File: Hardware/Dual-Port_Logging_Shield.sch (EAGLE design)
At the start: 87 parts, among them IC1 USB224X_2241, J2 MICRO-SD-PUSH-PUSH-EXT-PIN, J3 AVR_SPI_PROG_3X2TESTPOINTS, J4 THING_PLUS, Q1 20V/4.2A/52mΩ/1.4W, Q2 20V/0.2A/8MHz/1.2Ω/1Vth, Q3 20V/4.2A/52mΩ/1.4W, Q4 20V/4.2A/52mΩ/1.4W, Q6 20V/4.2A/52mΩ/1.4W, U1 3.3V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

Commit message: Final Eagle files for Proto
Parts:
- added D+, D-, MICROSD_VCC, V_USB: TEST-POINT3, SparkFun-Connectors:TEST-POINT3
- added D3: PRTR5V0U2F, SparkFun-IC-Power:PRTR5V0U2F
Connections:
- new net D+_IN: D+.1, D3.6, J1.D+
- new net D-_IN: D-.1, D3.4, J1.D-
- net D+: now also D3.1; no longer J1.D+
- net D-: now also D3.3; no longer J1.D-
- net GND: now also D3.2
- net MICROSD_VCC: now also MICROSD_VCC.1
- net V_USB: now also D3.5, V_USB.1
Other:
- note added: "Default I2C Address (Unshifted): 0x51 Address is programmable"
- note added: "USB Differential Pair: Conductor Width: 8.8 mils Conductor Spacing (center to center): 15 mils Conductor Spacing (gap): 6.2 mils Prepreg Thickness: 0.2 mm (7.87 mils) Zdifferential: 90.1 Ohms https://saturnpcb.com/saturn-pcb-toolkit/"
- moved on the sheet: C13, C6, C7, D1, D2, GND, I2C, J1, J3, LED1, LED2, R10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

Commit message: Updates post proto review
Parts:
- added R26, R27, R28: 100, SparkFun-Resistors:100OHM-0402-TIGHT-1/16W-1%
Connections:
- removed net AT_CIPO: J3.1, U3.(CIPO/A5)5
- new net AT_POCI: J3.1, U3.(POCI/A5)5
- new net N$6: Q3.G, R26.2, R9.1
- new net N$7: Q2.G, R20.2, R27.1
- new net N$8: Q2.D, R28.1
- net MICROSD_PWR_EN: now also R26.1; no longer Q3.G, R9.1
- net N$17: now also R28.2; no longer Q2.D
- net SDA: now also U3.(SDA/PICO/A6)6; no longer U3.(SDA/COPI/A6)6
- net SDIO_EN: now also R27.2; no longer Q2.G, R20.2
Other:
- note added: "v01"
- note removed: "v10"
- moved on the sheet: C5, C9, J2, Q2, Q3, R15, R20, R9, U4

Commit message: Add v10 hardware files
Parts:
- removed SD_WP: TEST-POINT3, SparkFun-Connectors:TEST-POINT3
- added R29, R30: 10k, SparkFun-Resistors:10KOHM-0402T-1/16W-1%
- added SH: JUMPER-SMT_2_NC_TRACE_SILK, SparkFun-Jumpers:JUMPER-SMT_2_NC_TRACE_SILK
- D+, D-, GND, V_USB: value TEST-POINT3 -> TEST-POINT3X5; device SparkFun-Connectors:TEST-POINT3 -> SparkFun-Connectors:TEST-POINT3X5
- IC1: value USB224X_2241 -> USB224X_2241_V04; device USB224x:USB224X_2241 -> SparkFun-IC-Special-Function:USB224X_2241_V04
- R21, R23: value 10k -> 100k; device SparkFun-Resistors:10KOHM-0402T-1/16W-1% -> SparkFun-Resistors:100KOHM-0402T-1/16W-1%
- R22, R24: value 47k -> 1M; device SparkFun-Resistors:47KOHM-0402-1/10W-1% -> SparkFun-Resistors:1MOHM-0402T-1/16W-5%
- U2, U4, U5: device 74HC4066:74HC4066_QUAD_BILATERAL_SWITCH_QFN -> SparkFun-IC-Logic:74HC4066_QUAD_BILATERAL_SWITCH_QFN
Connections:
- removed net SD_WP: IC1.SD_WP, SD_WP.1
- new net N$12: J1.SHLD, SH.1
- new net N$20: IC1.SD_WP, R29.1
- net 3.3V: now also R30.1
- net GND: now also R29.2, SH.2
- net POCI: now also R30.2
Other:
- note added: "v10"
- note removed: "v01"
- moved on the sheet: C10, J4, JP1, JP2, JP3, R10, R11, RXD, TXD

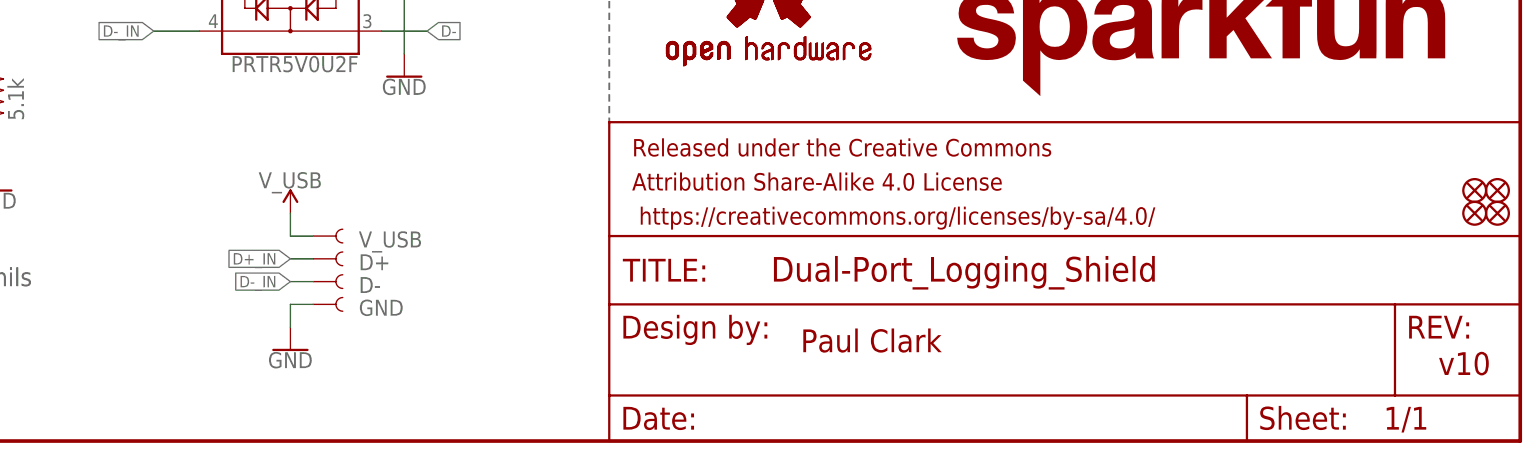
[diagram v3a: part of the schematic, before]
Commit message: Updated hardware files after REDS Review
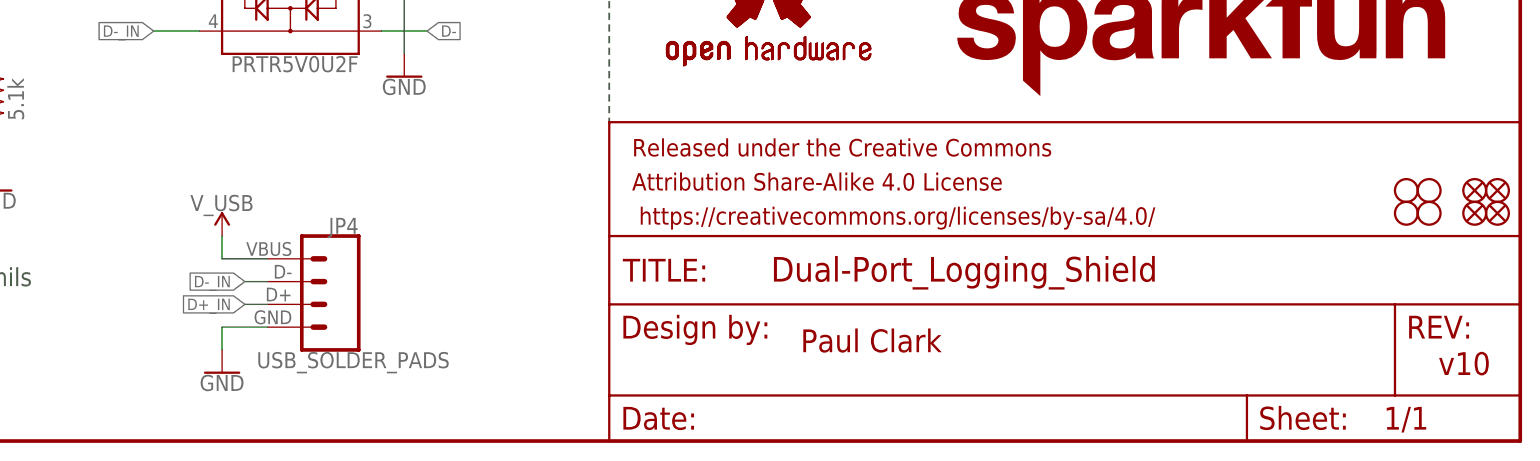
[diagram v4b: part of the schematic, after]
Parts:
- removed D+, D-, GND, V_USB: TEST-POINT3X5, SparkFun-Connectors:TEST-POINT3X5
- added H1, H2, H3, H4: STAND-OFF, SparkFun-Hardware:STAND-OFF
- added JP4: USB_SOLDER_PADS, SparkFun-Connectors:USB_SOLDER_PADS
- J4: device Thing_Plus:THING_PLUS -> SparkFun-Boards:THING_PLUS
- SH: value JUMPER-SMT_2_NC_TRACE_SILK -> JUMPER-SMT_2_NC_TRACE_NO-SILK; device SparkFun-Jumpers:JUMPER-SMT_2_NC_TRACE_SILK -> SparkFun-Jumpers:JUMPER-SMT_2_NC_TRACE_NO-SILK
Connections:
- net D+_IN: now also JP4.3; no longer D+.1
- net D-_IN: now also JP4.2; no longer D-.1
- net GND: now also JP4.4; no longer GND.1
- net V_USB: now also JP4.1; no longer V_USB.1
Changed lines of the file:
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@@
 <drawing>
 <settings>
-<setting alwaysvectorfont="yes"/>
+<setting alwaysvectorfont="no"/>
 <setting verticaltext="up"/>
 </settings>
@@
 <part name="Q3" library="SparkFun-DiscreteSemi" deviceset="MOSFET_PCH" device="-DMG2305UX-7" value="20V/4.2A/52mΩ/1.4W"/>
 <part name="R9" library="SparkFun-Resistors" deviceset="100KOHM" device="-0402T-1/16W-1%" value="100k"/>
-<part name="J4" library="Thing_Plus" deviceset="THING_PLUS" device=""/>
+<part name="J4" library="SparkFun-Boards" deviceset="THING_PLUS" device=""/>
 <part name="GND17" library="SparkFun-PowerSymbols" deviceset="GND" device=""/>
 <part name="SUPPLY2" library="SparkFun-PowerSymbols" deviceset="3.3V" device=""/>
@@
 <part name="GND32" library="SparkFun-PowerSymbols" deviceset="GND" device=""/>
 <part name="SDIO_VDD" library="SparkFun-Connectors" deviceset="TEST-POINT" device="3"/>
-<part name="GND" library="SparkFun-Connectors" deviceset="TEST-POINT" device="3X5" value="TEST-POINT3X5"/>
 <part name="RXD" library="SparkFun-Jumpers" deviceset="JUMPER-SMT_2_NO" device="_SILK" package3d_urn="urn:adsk.eagle:package:39279/1"/>
 <part name="TXD" library="SparkFun-Jumpers" deviceset="JUMPER-SMT_2_NO" device="_SILK" package3d_urn="urn:adsk.eagle:package:39279/1"/>
@@
 <part name="GND38" library="SparkFun-PowerSymbols" deviceset="GND" device=""/>
 <part name="GPIO10" library="SparkFun-Connectors" deviceset="TEST-POINT" device="3"/>
-<part name="D+" library="SparkFun-Connectors" deviceset="TEST-POINT" device="3X5" value="TEST-POINT3X5"/>
-<part name="D-" library="SparkFun-Connectors" deviceset="TEST-POINT" device="3X5" value="TEST-POINT3X5"/>
-<part name="V_USB" library="SparkFun-Connectors" deviceset="TEST-POINT" device="3X5" value="TEST-POINT3X5"/>
 <part name="SUPPLY9" library="SparkFun-PowerSymbols" deviceset="V_USB" device=""/>
 <part name="MICROSD_VCC" library="SparkFun-Connectors" deviceset="TEST-POINT" device="3"/>
@@
 <part name="R27" library="SparkFun-Resistors" deviceset="100OHM" device="-0402-TIGHT-1/16W-1%" value="100"/>
 <part name="R28" library="SparkFun-Resistors" deviceset="100OHM" device="-0402-TIGHT-1/16W-1%" value="100"/>
-<part name="SH" library="SparkFun-Jumpers" deviceset="JUMPER-SMT_2_NC_TRACE" device="_SILK" package3d_urn="urn:adsk.eagle:package:39281/1"/>
+<part name="SH" library="SparkFun-Jumpers" deviceset="JUMPER-SMT_2_NC_TRACE" device="_NO-SILK" package3d_urn="urn:adsk.eagle:package:39286/1"/>
 <part name="GND41" library="SparkFun-PowerSymbols" deviceset="GND" device=""/>
 <part name="R29" library="SparkFun-Resistors" deviceset="10KOHM" device="-0402T-1/16W-1%" value="10k"/>
@@
 <part name="R30" library="SparkFun-Resistors" deviceset="10KOHM" device="-0402T-1/16W-1%" value="10k"/>
 <part name="SUPPLY18" library="SparkFun-PowerSymbols" deviceset="3.3V" device=""/>
+<part name="H1" library="SparkFun-Hardware" deviceset="STAND-OFF" device=""/>
+<part name="H2" library="SparkFun-Hardware" deviceset="STAND-OFF" device=""/>
+<part name="H3" library="SparkFun-Hardware" deviceset="STAND-OFF" device=""/>
+<part name="H4" library="SparkFun-Hardware" deviceset="STAND-OFF" device=""/>
+<part name="JP4" library="SparkFun-Connectors" deviceset="USB_SOLDER_PADS" device=""/>
 </parts>
 <sheets>
@@
 <attribute name="NAME" x="171.45" y="226.06" size="1.778" layer="95" font="vector" rot="R90"/>
 </instance>
-<instance part="GND" gate="G$1" x="297.18" y="15.24" smashed="yes">
-<attribute name="NAME" x="302.26" y="13.97" size="1.778" layer="95" font="vector"/>
-</instance>
 <instance part="RXD" gate="G$1" x="60.96" y="48.26" smashed="yes">
 <attribute name="NAME" x="64.77" y="49.784" size="1.778" layer="95" font="vector" align="center"/>
@@
 <attribute name="NAME" x="256.54" y="208.28" size="1.778" layer="95" font="vector"/>
 </instance>
-<instance part="D+" gate="G$1" x="297.18" y="20.32" smashed="yes">
-<attribute name="NAME" x="302.26" y="19.05" size="1.778" layer="95" font="vector"/>
-</instance>
-<instance part="D-" gate="G$1" x="297.18" y="17.78" smashed="yes">
-<attribute name="NAME" x="302.26" y="16.51" size="1.778" layer="95" font="vector"/>
-</instance>
-<instance part="V_USB" gate="G$1" x="297.18" y="22.86" smashed="yes">
-<attribute name="NAME" x="302.26" y="21.59" size="1.778" layer="95" font="vector"/>
-</instance>
-<instance part="SUPPLY9" gate="G$1" x="294.64" y="25.4" smashed="yes">
-<attribute name="VALUE" x="294.64" y="28.194" size="1.778" layer="96" align="bottom-center"/>
+<instance part="SUPPLY9" gate="G$1" x="287.02" y="22.86" smashed="yes">
+<attribute name="VALUE" x="287.02" y="25.654" size="1.778" layer="96" align="bottom-center"/>
 </instance>
 <instance part="MICROSD_VCC" gate="G$1" x="60.96" y="104.14" smashed="yes" rot="R90"/>
-<instance part="GND39" gate="1" x="294.64" y="10.16" smashed="yes">
-<attribute name="VALUE" x="294.64" y="9.906" size="1.778" layer="96" align="top-center"/>
+<instance part="GND39" gate="1" x="287.02" y="7.62" smashed="yes">
+<attribute name="VALUE" x="287.02" y="7.366" size="1.778" layer="96" align="top-center"/>
 </instance>
 <instance part="D3" gate="D1" x="294.64" y="50.8" smashed="yes" rot="MR0">
@@
 <instance part="SUPPLY18" gate="G$1" x="73.66" y="22.86" smashed="yes">
 <attribute name="VALUE" x="73.66" y="25.654" size="1.778" layer="96" align="bottom-center"/>
+</instance>
+<instance part="H1" gate="G$1" x="419.1" y="27.94" smashed="yes"/>
+<instance part="H2" gate="G$1" x="421.64" y="27.94" smashed="yes"/>
+<instance part="H3" gate="G$1" x="421.64" y="25.4" smashed="yes"/>
+<instance part="H4" gate="G$1" x="419.1" y="25.4" smashed="yes"/>
+<instance part="JP4" gate="JP1" x="297.18" y="17.78" smashed="yes" rot="R180">
+<attribute name="VALUE" x="312.42" y="9.906" size="1.778" layer="96" font="vector" rot="R180"/>
+<attribute name="NAME" x="302.26" y="24.892" size="1.778" layer="95" font="vector" rot="R180"/>
 </instance>
 </instances>
@@
 </segment>
 <segment>
-<pinref part="GND" gate="G$1" pin="1"/>
-<wire x1="297.18" y1="15.24" x2="294.64" y2="15.24" width="0.1524" layer="91"/>
 <pinref part="GND39" gate="1" pin="GND"/>
-<wire x1="294.64" y1="15.24" x2="294.64" y2="12.7" width="0.1524" layer="91"/>
+<wire x1="287.02" y1="12.7" x2="287.02" y2="10.16" width="0.1524" layer="91"/>
+<pinref part="JP4" gate="JP1" pin="4"/>
+<wire x1="292.1" y1="12.7" x2="287.02" y2="12.7" width="0.1524" layer="91"/>
 </segment>
 <segment>
@@
 </segment>
 <segment>
-<pinref part="V_USB" gate="G$1" pin="1"/>
-<wire x1="297.18" y1="22.86" x2="294.64" y2="22.86" width="0.1524" layer="91"/>
 <pinref part="SUPPLY9" gate="G$1" pin="V_USB"/>
-<wire x1="294.64" y1="22.86" x2="294.64" y2="25.4" width="0.1524" layer="91"/>
+<wire x1="287.02" y1="20.32" x2="287.02" y2="22.86" width="0.1524" layer="91"/>
+<pinref part="JP4" gate="JP1" pin="1"/>
+<wire x1="292.1" y1="20.32" x2="287.02" y2="20.32" width="0.1524" layer="91"/>
 </segment>
 <segment>
@@
 </segment>
 <segment>
-<pinref part="D+" gate="G$1" pin="1"/>
-<wire x1="297.18" y1="20.32" x2="294.64" y2="20.32" width="0.1524" layer="91"/>
-<label x="294.64" y="20.32" size="1.27" layer="95" font="vector" rot="R180" xref="yes"/>
+<label x="289.56" y="15.24" size="1.27" layer="95" font="vector" rot="R180" xref="yes"/>
+<pinref part="JP4" gate="JP1" pin="3"/>
+<wire x1="292.1" y1="15.24" x2="289.56" y2="15.24" width="0.1524" layer="91"/>
 </segment>
 <segment>
@@
 </segment>
 <segment>
-<pinref part="D-" gate="G$1" pin="1"/>
-<wire x1="297.18" y1="17.78" x2="294.64" y2="17.78" width="0.1524" layer="91"/>
-<label x="294.64" y="17.78" size="1.27" layer="95" font="vector" rot="R180" xref="yes"/>
-</segment>
-<segment>
+<label x="289.56" y="17.78" size="1.27" layer="95" font="vector" rot="R180" xref="yes"/>
+<pinref part="JP4" gate="JP1" pin="2"/>
+<wire x1="292.1" y1="17.78" x2="289.56" y2="17.78" width="0.1524" layer="91"/>
+</segment>
+<segment>

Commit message: PCB v1.1
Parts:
- added C20, C21, C22, C23, C24: 10uF, SparkFun-Capacitors:10UF-0402T-6.3V-20%
- I2C: value JUMPER-SMT_3_NO_SILK -> JUMPER-SMT_3_2-NC_TRACE_SILK; device SparkFun-Jumpers:JUMPER-SMT_3_NO_SILK -> SparkFun-Jumpers:JUMPER-SMT_3_2-NC_TRACE_SILK
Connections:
- net GND: now also C20.2, C21.2, C22.2, C23.2, C24.2
- net VCC: now also C20.1, C21.1, C22.1, C23.1, C24.1
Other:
- note added: "Open split pads to disable I2C pull-ups (This will also help prevent the shield back-feeding power to the Thing Plus)"
- note added: "v11"
- note removed: "Close split pads to enable I2C pull-ups (Be aware that VCC will then try to back-feed power to the Thing Plus)"
- note removed: "v10"
- moved on the sheet: C11, C8, R18, R19
